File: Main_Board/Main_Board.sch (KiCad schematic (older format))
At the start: 67 parts, among them J1 Conn_01x06, J10 HR-SR04_L_CONN, J11 12V_OUT, J12 BATT_REG_IN, J13 LED_CONN, J14 PD_CONN, J2 Conn_01x06, J3 Conn_01x06, J4 BATT_IN, J5 Conn_02x08_Top_Bottom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

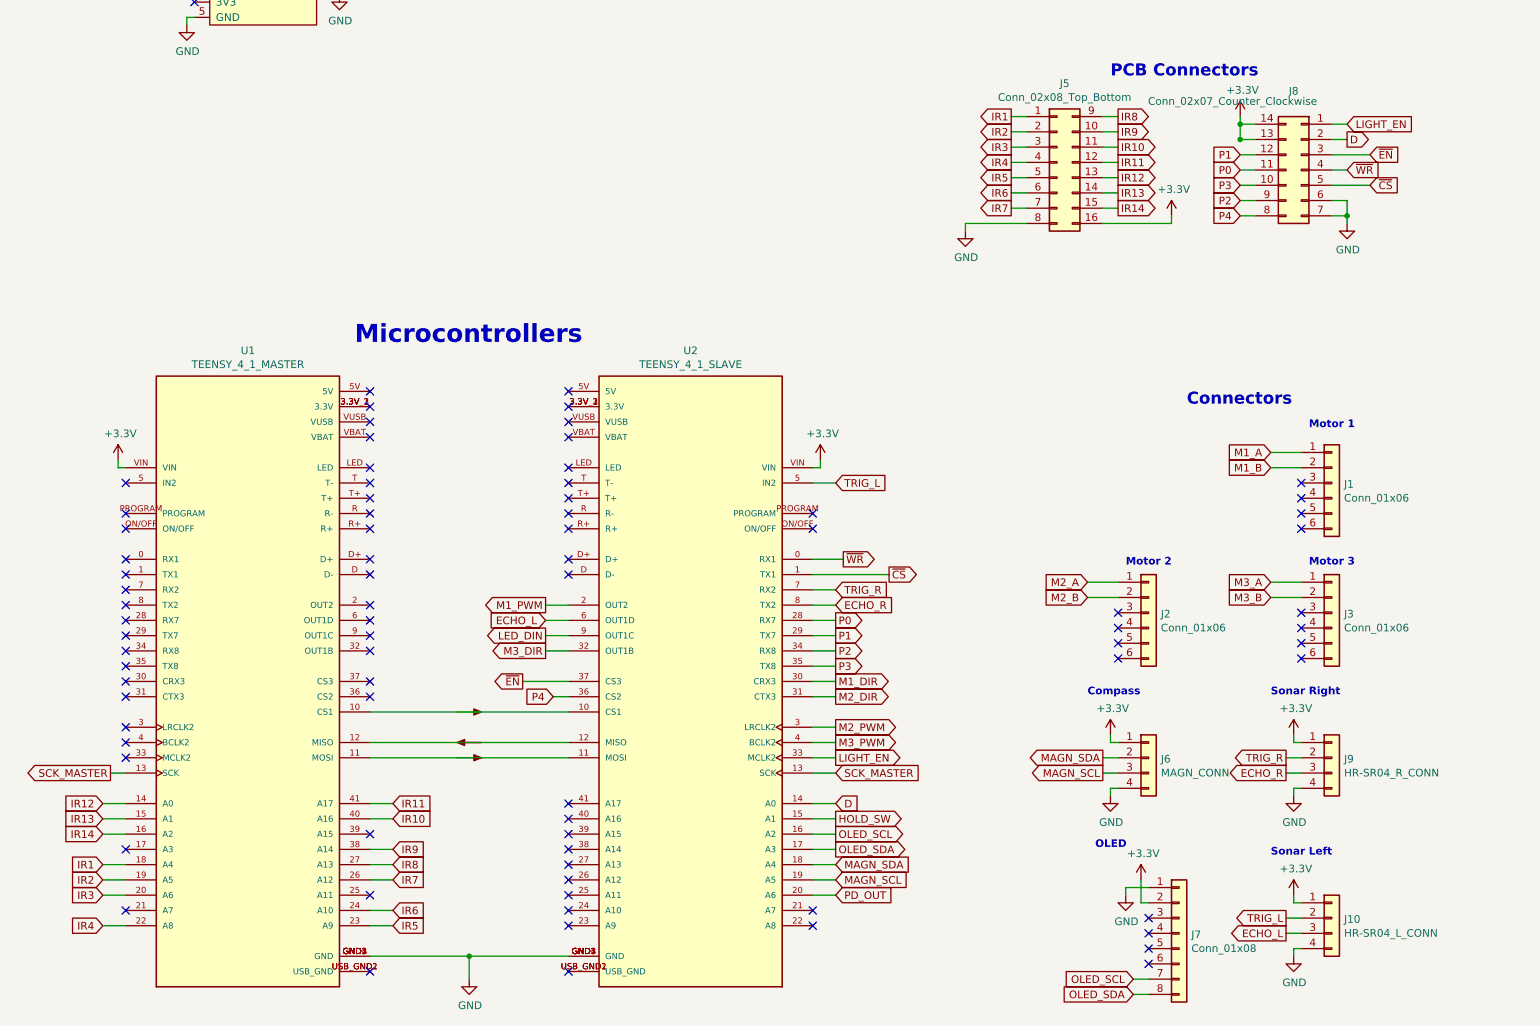
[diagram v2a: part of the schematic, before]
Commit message: Finished main part traces [MAIN_PCB]
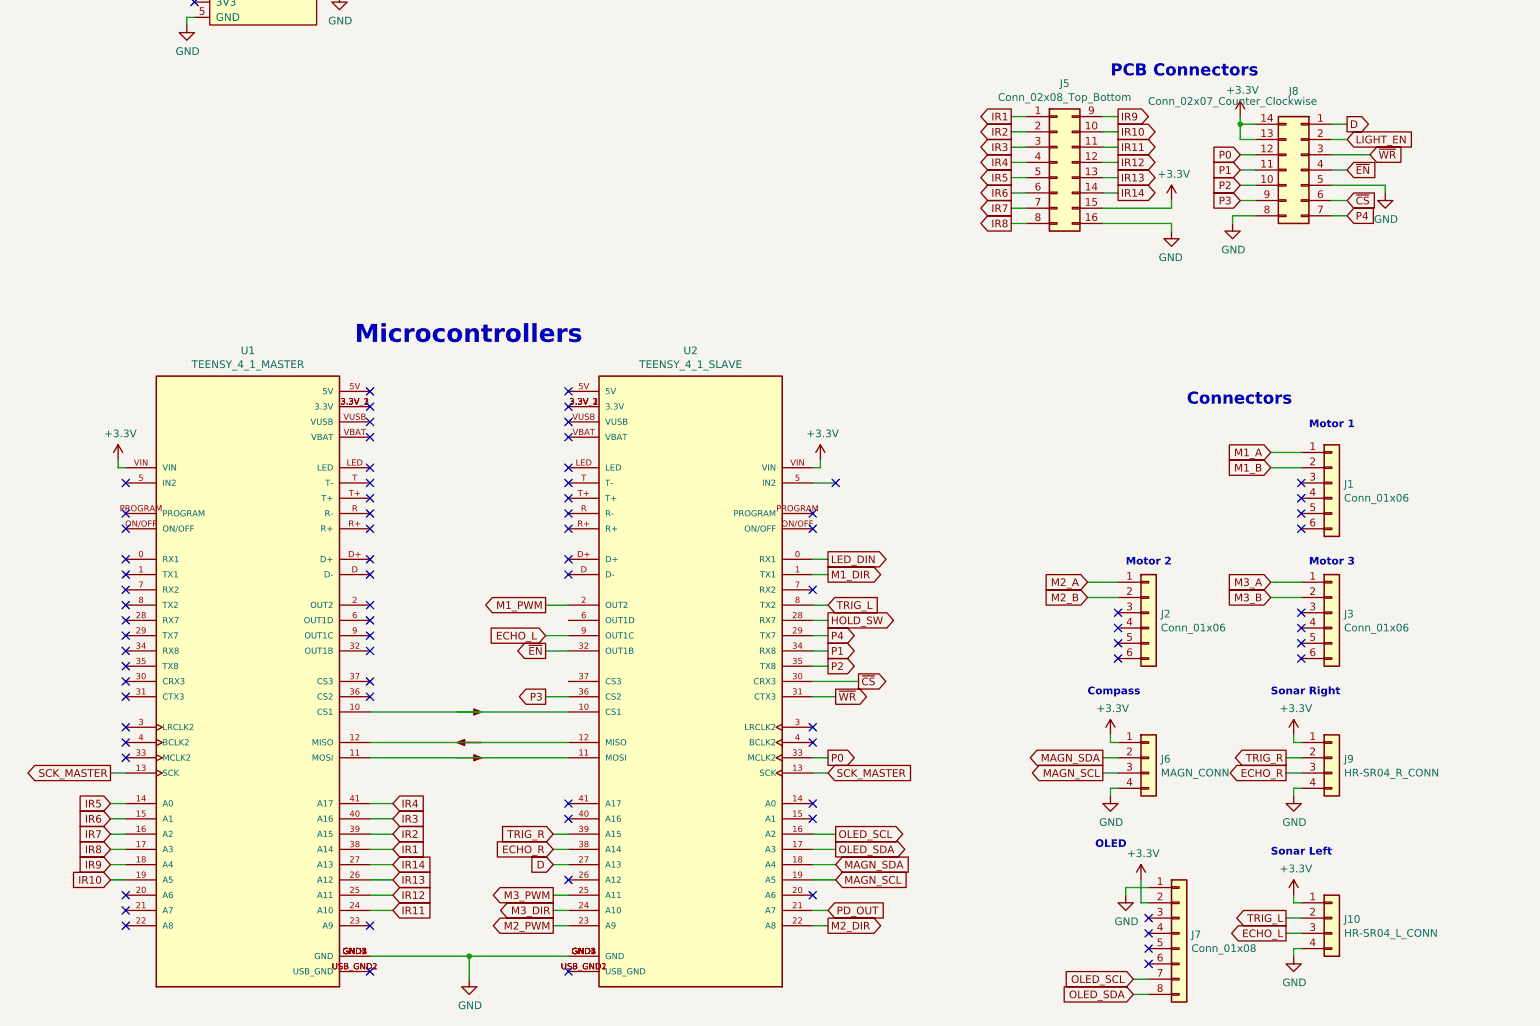
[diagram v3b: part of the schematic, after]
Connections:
- net +3V3: now also J5.15 (Pin_15); no longer J5.16 (Pin_16)
- net D: now also J8.1 (Pin_1), U2.27 (A13); no longer J8.2 (Pin_2), U2.14 (A0)
- net ECHO_L: now also U2.9 (OUT1C); no longer U2.6 (OUT1D)
- net ECHO_R: now also U2.38 (A14); no longer U2.8 (TX2)
- net GND: now also J5.16 (Pin_16), J8.5 (Pin_5), J8.8 (Pin_8); no longer J5.8 (Pin_8), J8.6 (Pin_6), J8.7 (Pin_7)
- net HOLD_SW: now also U2.28 (RX7); no longer U2.15 (A1)
- net IR1: now also U1.38 (A14); no longer U1.18 (A4)
- net IR10: now also J5.10 (Pin_10), U1.19 (A5); no longer J5.11 (Pin_11), U1.40 (A16)
- net IR11: now also J5.11 (Pin_11), U1.24 (A10); no longer J5.12 (Pin_12), U1.41 (A17)
- net IR12: now also J5.12 (Pin_12), U1.25 (A11); no longer J5.13 (Pin_13), U1.14 (A0)
- net IR13: now also J5.13 (Pin_13), U1.26 (A12); no longer J5.14 (Pin_14), U1.15 (A1)
- net IR14: now also J5.14 (Pin_14), U1.27 (A13); no longer J5.15 (Pin_15), U1.16 (A2)
- net IR2: now also U1.39 (A15); no longer U1.19 (A5)
- net IR3: now also U1.40 (A16); no longer U1.20 (A6)
- net IR4: now also U1.41 (A17); no longer U1.22 (A8)
- net IR5: now also U1.14 (A0); no longer U1.23 (A9)
- net IR6: now also U1.15 (A1); no longer U1.24 (A10)
- net IR7: now also U1.16 (A2); no longer U1.26 (A12)
- net IR8: now also J5.8 (Pin_8), U1.17 (A3); no longer J5.9 (Pin_9), U1.27 (A13)
- net IR9: now also J5.9 (Pin_9), U1.18 (A4); no longer J5.10 (Pin_10), U1.38 (A14)
- net LED_DIN: now also U2.0 (RX1); no longer U2.9 (OUT1C)
- net LIGHT_EN: now also J8.2 (Pin_2); no longer J8.1 (Pin_1), U2.33 (MCLK2)
- net M1_DIR: now also U2.1 (TX1); no longer U2.30 (CRX3)
- net M2_DIR: now also U2.22 (A8); no longer U2.31 (CTX3)
- net M2_PWM: now also U2.23 (A9); no longer U2.3 (LRCLK2)
- net M3_DIR: now also U2.24 (A10); no longer U2.32 (OUT1B)
- net M3_PWM: now also U2.25 (A11); no longer U2.4 (BCLK2)
- net P0: now also J8.12 (Pin_12), U2.33 (MCLK2); no longer J8.11 (Pin_11), U2.28 (RX7)
- net P1: now also J8.11 (Pin_11), U2.34 (RX8); no longer J8.12 (Pin_12), U2.29 (TX7)
- net P2: now also J8.10 (Pin_10), U2.35 (TX8); no longer J8.9 (Pin_9), U2.34 (RX8)
- net P3: now also J8.9 (Pin_9), U2.36 (CS2); no longer J8.10 (Pin_10), U2.35 (TX8)
- net P4: now also J8.7 (Pin_7), U2.29 (TX7); no longer J8.8 (Pin_8), U2.36 (CS2)
- net PD_OUT: now also U2.21 (A7); no longer U2.20 (A6)
- net TRIG_L: now also U2.8 (TX2); no longer U2.5 (IN2)
- net TRIG_R: now also U2.39 (A15); no longer U2.7 (RX2)
- net ~CS: now also J8.6 (Pin_6), U2.30 (CRX3); no longer J8.5 (Pin_5), U2.1 (TX1)
- net ~EN: now also J8.4 (Pin_4), U2.32 (OUT1B); no longer J8.3 (Pin_3), U2.37 (CS3)
- net ~WR: now also J8.3 (Pin_3), U2.31 (CTX3); no longer J8.4 (Pin_4), U2.0 (RX1)
- no-connect marks 97 -> 96

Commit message: Finished board [MAIN BOARD]
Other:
- moved on the sheet: D12
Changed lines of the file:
@@
 Connection ~ 14900 3950
 Wire Wire Line
-	10100 3100 10150 3100
-Wire Wire Line
-	9900 3100 9850 3100
-Wire Wire Line
-	9850 3100 9850 1900
+	9850 3100 9850 2950
 Connection ~ 9850 1900
 Wire Wire Line
@@
 L Device:D_Zener_Small D12
 U 1 1 62959DA5
-P 10000 3100
-F 0 "D12" H 10000 2893 50  0000 C CNN
-F 1 "20V" H 10000 2984 50  0000 C CNN
-F 2 "Diode_SMD:D_SOD-123" V 10000 3100 50  0001 C CNN
-F 3 "~" V 10000 3100 50  0001 C CNN
-	1    10000 3100
-	1    0    0    1
+P 9850 2850
+F 0 "D12" H 9850 2643 50  0000 C CNN
+F 1 "20V" H 9850 2734 50  0000 C CNN
+F 2 "Diode_SMD:D_SOD-123" V 9850 2850 50  0001 C CNN
+F 3 "~" V 9850 2850 50  0001 C CNN
+	1    9850 2850
+	0    -1   1    0
 $EndComp
 NoConn ~ 9500 7400
@@
 	4600 9900 4700 9900
 NoConn ~ 4700 10000
+Wire Wire Line
+	9850 2750 9850 1900
+Wire Wire Line
+	9850 3100 10150 3100
 $EndSCHEMATC

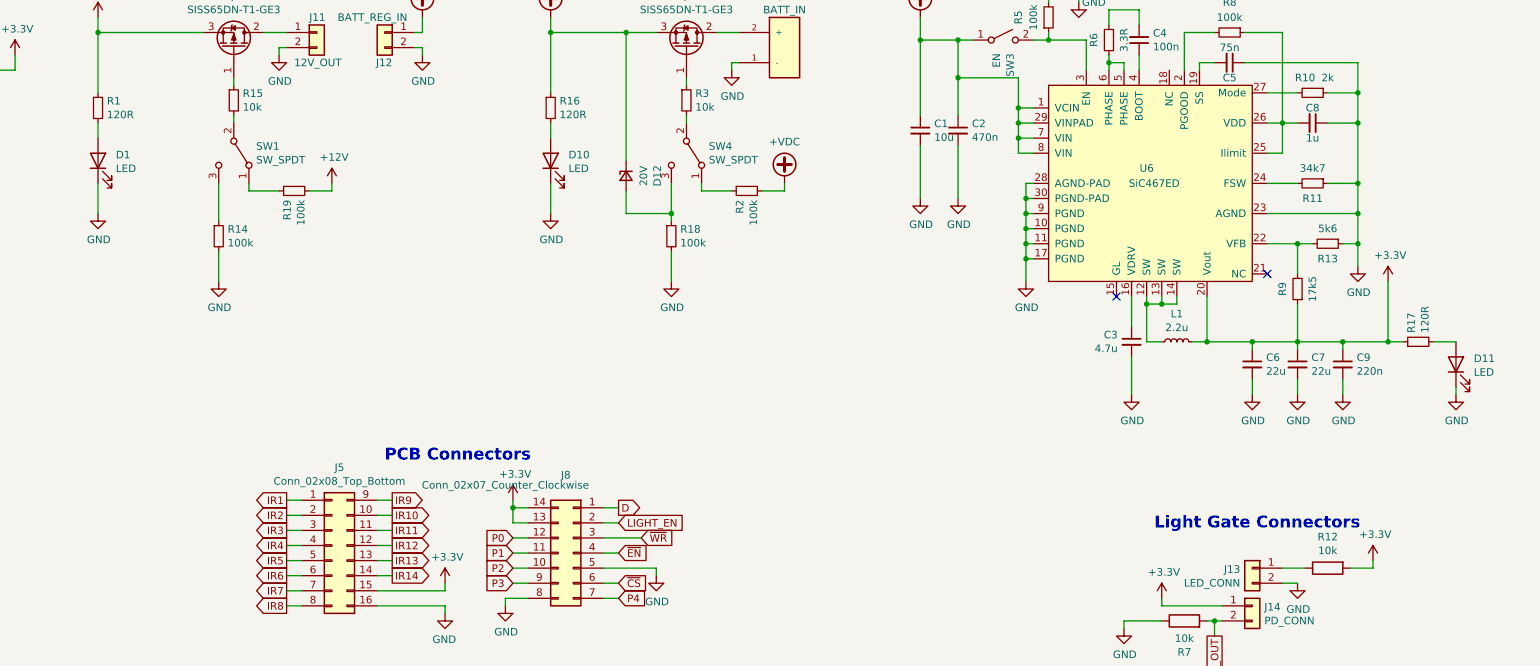
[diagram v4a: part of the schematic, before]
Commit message: Finished DRC [MAIN BOARD]
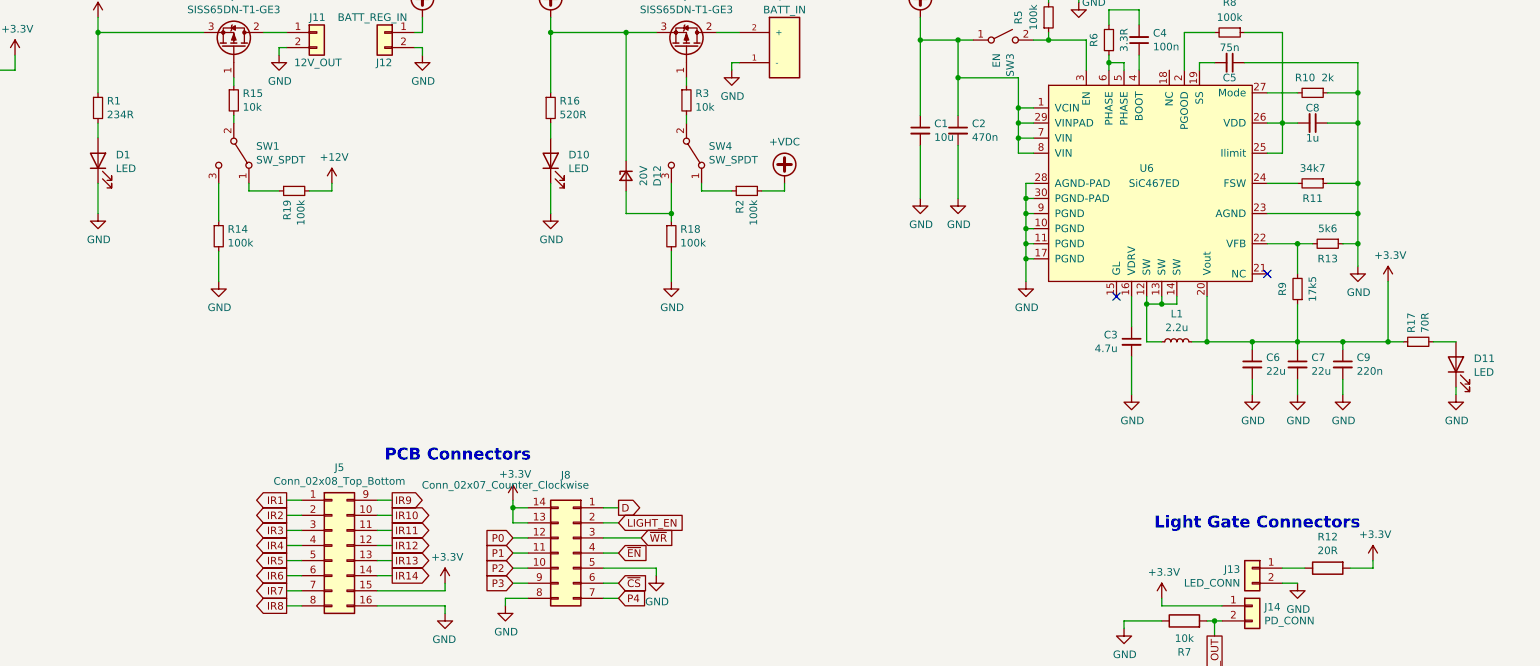
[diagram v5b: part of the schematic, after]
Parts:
- R1: value 120R -> 234R
- R12: value 10k -> 20R
- R16: value 120R -> 520R
- R17: value 120R -> 70R
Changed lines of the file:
@@
 P 14500 5450
 F 0 "R12" V 14293 5450 50  0000 C CNN
-F 1 "10k" V 14384 5450 50  0000 C CNN
+F 1 "20R" V 14384 5450 50  0000 C CNN
 F 2 "Resistor_SMD:R_0805_2012Metric" V 14430 5450 50  0001 C CNN
 F 3 "~" H 14500 5450 50  0001 C CNN
@@
 P 9350 2400
 F 0 "R16" H 9409 2446 50  0000 L CNN
-F 1 "120R" H 9409 2355 50  0000 L CNN
+F 1 "520R" H 9409 2355 50  0000 L CNN
 F 2 "Resistor_SMD:R_0603_1608Metric" H 9350 2400 50  0001 C CNN
 F 3 "~" H 9350 2400 50  0001 C CNN
@@
 P 15100 3950
 F 0 "R17" H 15159 3996 50  0000 L CNN
-F 1 "120R" H 15159 3905 50  0000 L CNN
+F 1 "70R" H 15159 3905 50  0000 L CNN
 F 2 "Resistor_SMD:R_0603_1608Metric" H 15100 3950 50  0001 C CNN
 F 3 "~" H 15100 3950 50  0001 C CNN
@@
 P 6350 2400
 F 0 "R1" H 6409 2446 50  0000 L CNN
-F 1 "120R" H 6409 2355 50  0000 L CNN
+F 1 "234R" H 6409 2355 50  0000 L CNN
 F 2 "Resistor_SMD:R_0603_1608Metric" H 6350 2400 50  0001 C CNN
 F 3 "~" H 6350 2400 50  0001 C CNN
@@
 Wire Wire Line
 	7150 3350 7150 3550
-Wire Wire Line
-	6350 1900 7050 1900
 Wire Wire Line
 	7150 2900 7150 3150
@@
 Wire Wire Line
 	9850 3100 10150 3100
+Wire Wire Line
+	6350 1900 7050 1900
 $EndSCHEMATC
